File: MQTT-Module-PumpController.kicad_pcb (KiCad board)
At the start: 4 copper layers, 44 x 55.9 mm, 33 parts, among them IC801 LM5060MMX_NOPB, J301 A2541WV-10P, J302 A2541WV-10P, J303 1715721, J304 A2541HWV-3P, Q801 60V 38A, U201 ATtiny1614-SS

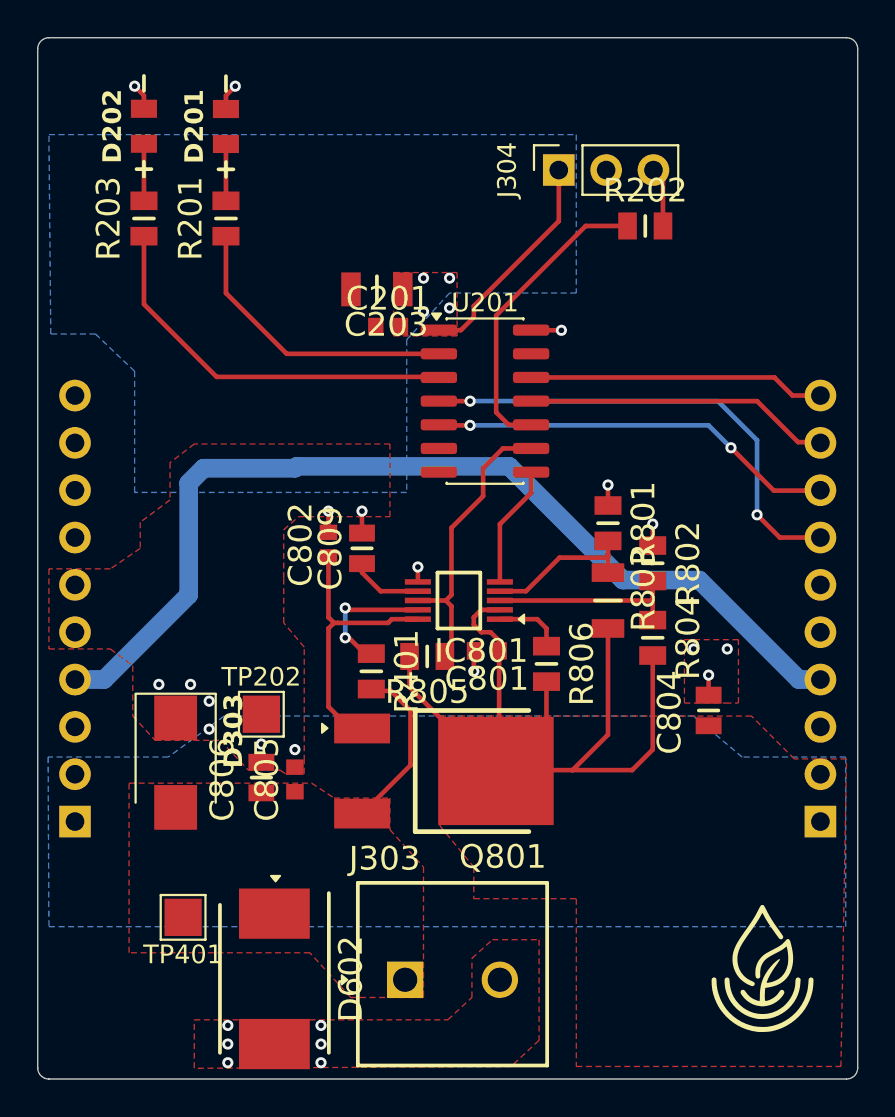
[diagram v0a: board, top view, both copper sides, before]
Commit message: Updated silkscreen.
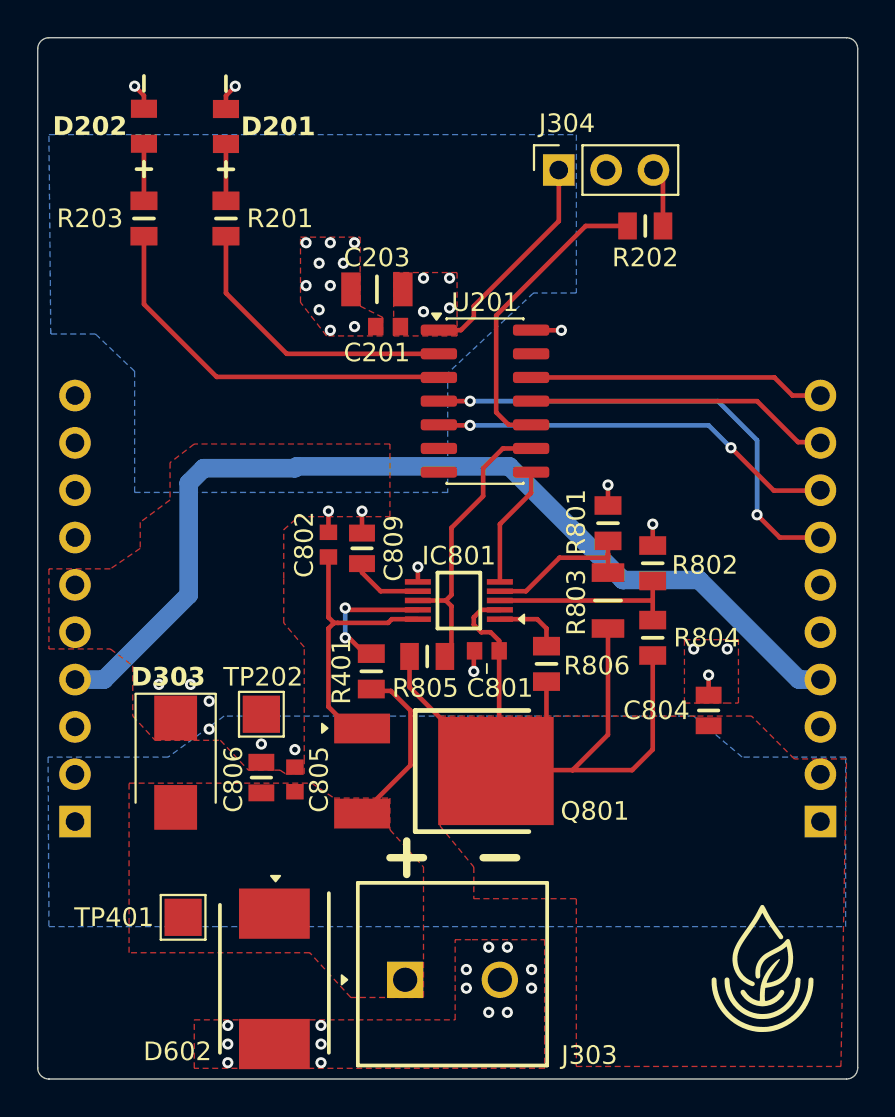
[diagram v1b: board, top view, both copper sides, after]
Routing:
- net GND: vias 24 -> 42

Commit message: Updated and completed base schematic and pcb. Added Reset Button.
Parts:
- added C205: 0.1uF 10% 50V, JLCPCB Basic:CAPC1608X90N, F.Cu at (153.3, 74.8)
- added R204: 10kΩ 1/8W 1%, JLCPCB Basic:RESC2013X65N, F.Cu at (150.0, 77.9)
- added S201: Push Button SPST, JLCPCB Basic:SW_TS-1088-AR02016, F.Cu at (156.5, 74.9)
- moved J304 5.24 mm to (141.4, 72.6)
- moved R202 5.10 mm to (145.5, 77.9)
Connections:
- U201 pad 13: unconnected-(U201-PA3-Pad13) -> /Controller/RESET
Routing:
- net /Controller/RESET: track 0.00 -> 24.3 mm
- net +3V3: track 65.0 -> 70.7 mm, vias 4 -> 5
- net /Controller/UDPI_C: track 3.21 -> 7.60 mm
- net /Controller/UPDI: track 16.4 -> 13.2 mm
- net GND: track 11.9 -> 14.2 mm, vias 42 -> 44
- net +12V: vias 0 -> 18
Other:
- board text added: "RESET"
- board text added: "github.com/WiddleWabbit/ MQTT-Module-PumpController"
- board text removed: "github.com/WiddleWabbit/ #####-#####-#####"

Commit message: Finalised silkscreen. Generated outputs.
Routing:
- net /Controller/UDPI_C: track 7.60 -> 5.30 mm
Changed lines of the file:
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@@
 		(tags "Diode SMB (DO-214AA)")
 		(property "Reference" "D303"
-			(at -4.6 0.4 180)
+			(at -4.7 0.4 180)
 			(layer "F.SilkS")
 			(effects
@@
 		(tags "test point SMD pad rectangle square")
 		(property "Reference" "TP202"
-			(at 0.1 -1.998 0)
+			(at 0.1 -2.1 0)
 			(layer "F.SilkS")
 			(effects
@@
 		(width 0.25)
 		(layer "F.Cu")
-		(net 24)
-	)
-	(segment
-		(start 146.44 72.6)
-		(end 146.44 74.9)
-		(width 0.25)
-		(layer "F.Cu")
